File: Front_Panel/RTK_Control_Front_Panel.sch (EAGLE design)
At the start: 11 parts

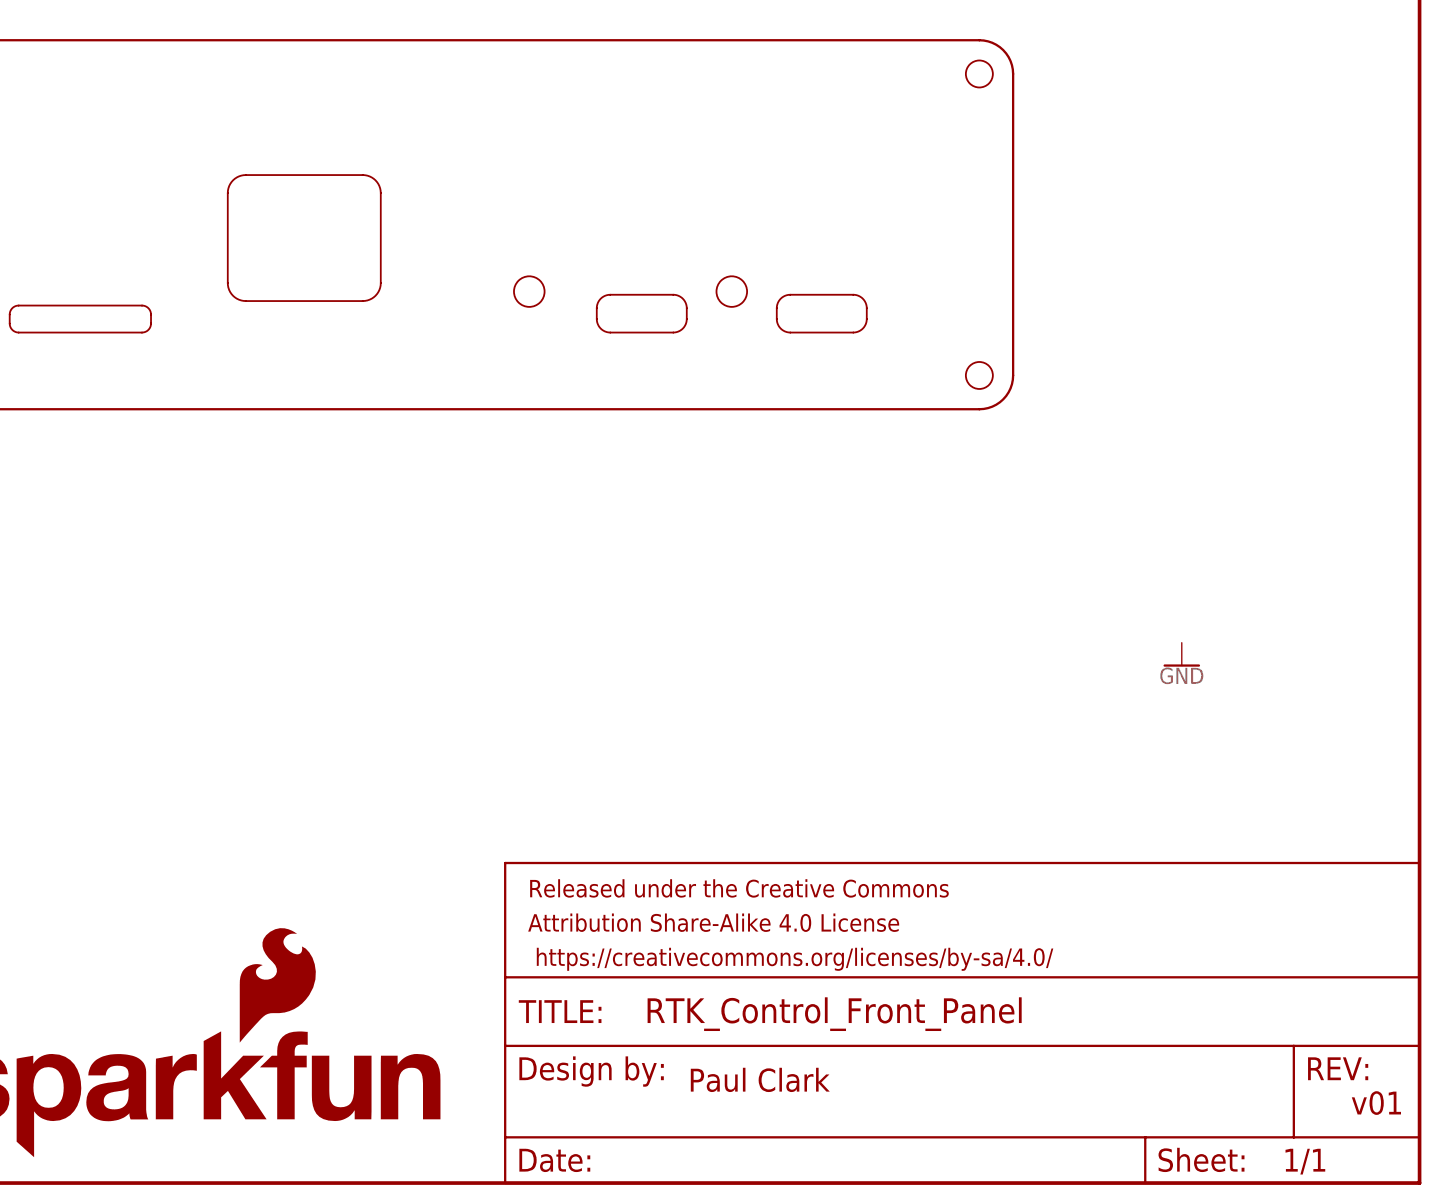
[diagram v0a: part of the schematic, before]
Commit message: Add 1.3" OLED
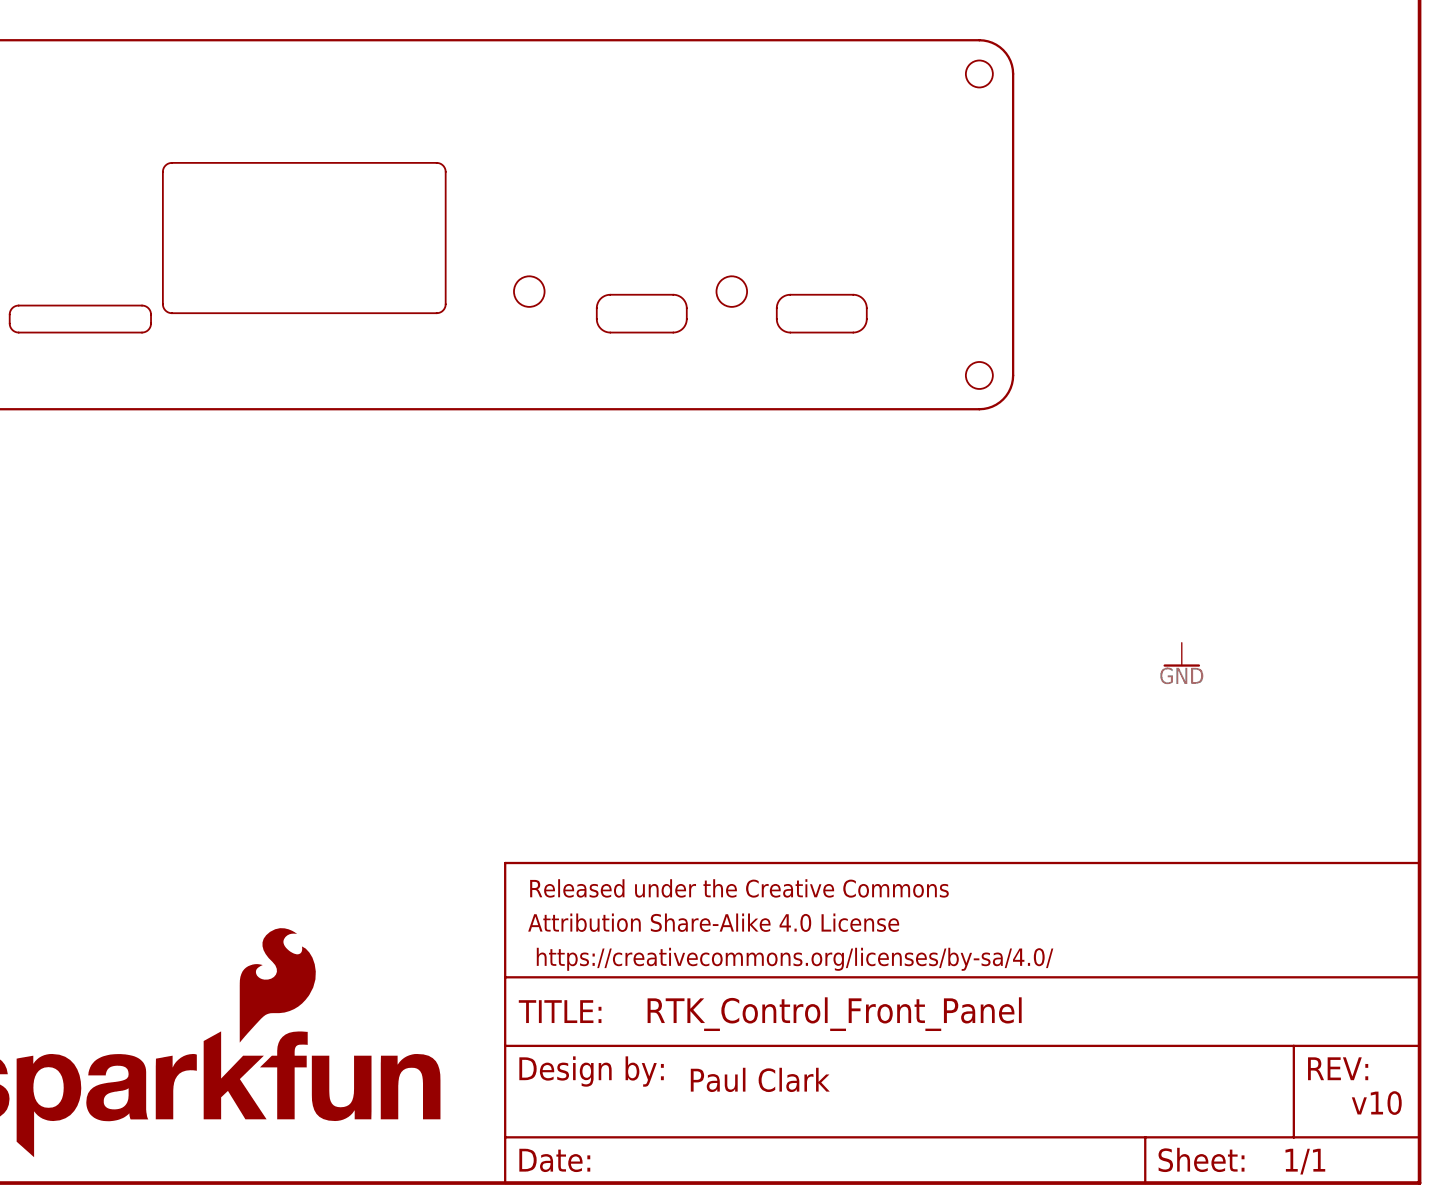
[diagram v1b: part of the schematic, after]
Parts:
- OLED: value OLED_14532 -> OLED_1.3_128X64; device SparkFun-Enclosure-Panel:OLED_14532 -> SparkFun-Enclosure-Panel:OLED_1.3_128X64
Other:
- note added: "v10"
- note removed: "v01"
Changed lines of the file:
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@@
 <layer number="154" name="FabDoc2" color="7" fill="1" visible="no" active="no"/>
 <layer number="155" name="FabDoc3" color="7" fill="1" visible="no" active="no"/>
+<layer number="156" name="gesam-Maß" color="1" fill="7" visible="no" active="no"/>
+<layer number="157" name="FaceMchng" color="3" fill="1" visible="no" active="no"/>
+<layer number="158" name="FaceMMeas" color="3" fill="1" visible="no" active="no"/>
+<layer number="159" name="Geh-Bear2" color="1" fill="7" visible="no" active="no"/>
+<layer number="160" name="Topologie" color="9" fill="1" visible="no" active="no"/>
+<layer number="161" name="tomplace2" color="7" fill="1" visible="no" active="no"/>
 <layer number="166" name="AntennaArea" color="7" fill="1" visible="no" active="no"/>
 <layer number="168" name="4mmHeightArea" color="7" fill="1" visible="no" active="no"/>
@@
 <layer number="250" name="Descript" color="3" fill="1" visible="no" active="no"/>
 <layer number="251" name="SMDround" color="12" fill="11" visible="no" active="no"/>
+<layer number="252" name="BR-BS" color="7" fill="1" visible="no" active="no"/>
 <layer number="253" name="Extra" color="7" fill="1" visible="no" active="no"/>
 <layer number="254" name="cooling" color="7" fill="1" visible="no" active="no"/>
@@
 <part name="ESP32_USB" library="SparkFun-Enclosure-Panel" deviceset="USB-C_CONN-14122" device=""/>
 <part name="GNSS_USB" library="SparkFun-Enclosure-Panel" deviceset="USB-C_CONN-14122" device=""/>
-<part name="OLED" library="SparkFun-Enclosure-Panel" deviceset="OLED_14532" device=""/>
+<part name="OLED" library="SparkFun-Enclosure-Panel" deviceset="OLED_1.3_128X64" device=""/>
 <part name="LOGO1" library="SparkFun-Aesthetics" deviceset="SFE_LOGO_NAME_FLAME" device=".3_INCH" value="SFE_LOGO_NAME_FLAME.3_INCH"/>
 <part name="U$3" library="SparkFun-Enclosure-Panel" deviceset="NANO_SIM_CONN-16272" device=""/>
@@
 <sheet>
 <plain>
-<text x="241.3" y="7.62" size="2.54" layer="94" font="vector">v01</text>
+<text x="241.3" y="7.62" size="2.54" layer="94" font="vector">v10</text>
 <text x="167.64" y="10.16" size="2.54" layer="94" font="vector">Paul Clark</text>
 </plain>
